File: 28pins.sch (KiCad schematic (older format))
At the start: 2 parts

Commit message: Adds 10-pin SIP header, BOM data to components
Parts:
- removed U?: ATMEGA16U2, symbol ATMEGA16U2
- added U?: ATMEGA16U2-AU, 28pins:TQFP-32_7x7mm_Pitch0.8mm, symbol ATMEGA16U2-AU
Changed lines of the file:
@@
 LIBS:valves
 LIBS:28pins
+LIBS:28pins-cache
 EELAYER 25 0
 EELAYER END
@@
 $EndComp
 $Comp
-L ATMEGA16U2 U?
-U 1 1 583FCE18
-P 11075 9775
-F 0 "U?" H 12125 9300 60  0000 C CNN
-F 1 "ATMEGA16U2" H 11025 9300 60  0000 C CNN
-F 2 "" H 12475 11075 60  0001 C CNN
-F 3 "" H 12475 11075 60  0001 C CNN
-	1    11075 9775
+L ATMEGA16U2-AU U?
+U 1 1 5840678A
+P 11525 9700
+F 0 "U?" H 12575 9225 60  0000 C CNN
+F 1 "ATMEGA16U2-AU" H 11475 9225 60  0000 C CNN
+F 2 "28pins:TQFP-32_7x7mm_Pitch0.8mm" H 11775 9025 60  0001 C CNN
+F 3 "http://www.atmel.com/Images/7799s.pdf" H 11750 8775 60  0001 C CNN
+F 4 "ATMEGA16U2-AU" H 11750 8575 60  0001 C CNN "MFG P/N"
+F 5 "Atmel" H 11100 8575 60  0001 C CNN "MFG"
+	1    11525 9700
 	1    0    0    -1
 $EndComp

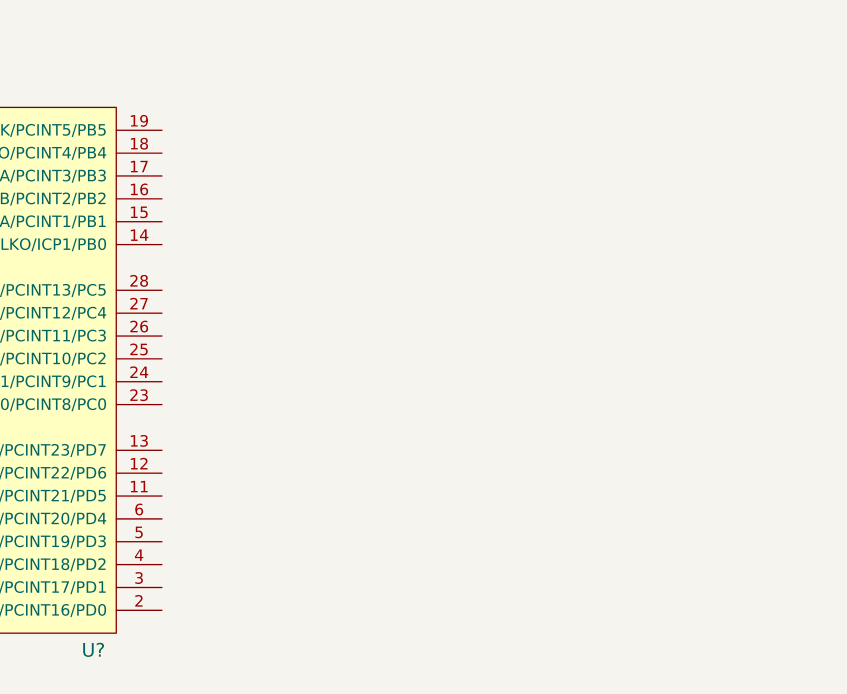
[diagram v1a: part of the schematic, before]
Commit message: Adds more headers and an 0805 capacitor
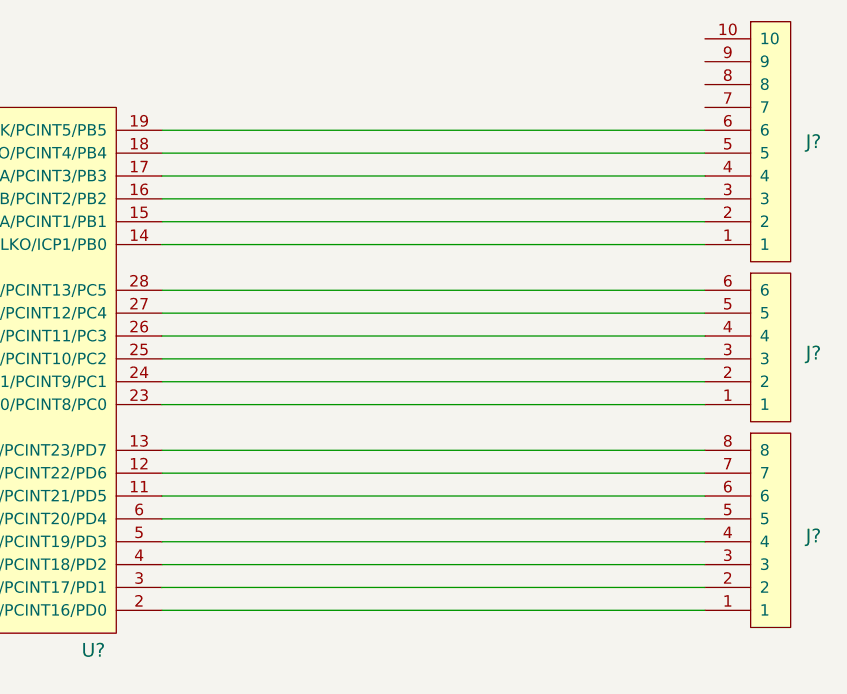
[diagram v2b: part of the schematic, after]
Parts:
- added J?: 10x1F, 28pins:1x10F_hdr, symbol 10x1F
- added J?: 8x1F, 28pins:1x10F_hdr, symbol 8x1F
- added J?: 6x1F, 28pins:1x6F_hdr, symbol 6x1F
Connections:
- net at U?.11 (OC0B/T1/PCINT21/PD5): now also J?.6
- net at U?.12 (OC0A/AIN0/PCINT22/PD6): now also J?.7
- net at U?.13 (AIN1/PCINT23/PD7): now also J?.8
- net at U?.14 (PCINT0/CLKO/ICP1/PB0): now also J?.1
- net at U?.15 (OC1A/PCINT1/PB1): now also J?.2
- net at U?.16 (SS/OC1B/PCINT2/PB2): now also J?.3
- net at U?.17 (MOSI/OC2A/PCINT3/PB3): now also J?.4
- net at U?.18 (MISO/PCINT4/PB4): now also J?.5
- net at U?.19 (SCK/PCINT5/PB5): now also J?.6
- net at U?.2 (RXD/PCINT16/PD0): now also J?.1
- net at U?.23 (ADC0/PCINT8/PC0): now also J?.1
- net at U?.24 (ADC1/PCINT9/PC1): now also J?.2
- net at U?.25 (ADC2/PCINT10/PC2): now also J?.3
- net at U?.26 (ADC3/PCINT11/PC3): now also J?.4
- net at U?.27 (ADC4/SDA/PCINT12/PC4): now also J?.5
- net at U?.28 (ADC5/SCL/PCINT13/PC5): now also J?.6
- net at U?.3 (TXD/PCINT17/PD1): now also J?.2
- net at U?.4 (INT0/PCINT18/PD2): now also J?.3
- net at U?.5 (OC2B/INT1/PCINT19/PD3): now also J?.4
- net at U?.6 (XCK/T0/PCINT20/PD4): now also J?.5
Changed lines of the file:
@@
 	1    0    0    -1
 $EndComp
+$Comp
+L 10x1F J?
+U 1 1 58410F8F
+P 20825 7675
+F 0 "J?" H 21100 7900 60  0000 C CNN
+F 1 "10x1F" H 20900 8475 60  0001 C CNN
+F 2 "28pins:1x10F_hdr" H 20800 7200 60  0001 C CNN
+F 3 "https://cdn.harwin.com/pdfs/M20-782.pdf" H 21025 6975 60  0001 C CNN
+F 4 "Harwin" H 20875 7075 60  0001 C CNN "MFG"
+F 5 "M20-7821042" H 21500 7075 60  0001 C CNN "MFG P/N"
+	1    20825 7675
+	1    0    0    1
+$EndComp
+$Comp
+L 8x1F J?
+U 1 1 58411004
+P 20825 9275
+F 0 "J?" H 21100 9625 60  0000 C CNN
+F 1 "8x1F" H 20900 10075 60  0001 C CNN
+F 2 "28pins:1x10F_hdr" H 20800 8800 60  0001 C CNN
+F 3 "https://cdn.harwin.com/pdfs/M20-782.pdf" H 21025 8575 60  0001 C CNN
+F 4 "Harwin" H 20875 8675 60  0001 C CNN "MFG"
+F 5 "M20-7820842" H 21500 8675 60  0001 C CNN "MFG P/N"
+	1    20825 9275
+	1    0    0    1
+$EndComp
+$Comp
+L 6x1F J?
+U 1 1 584110C3
+P 20825 8375
+F 0 "J?" H 21100 8825 60  0000 C CNN
+F 1 "6x1F" H 20900 9175 60  0001 C CNN
+F 2 "28pins:1x6F_hdr" H 20800 7900 60  0001 C CNN
+F 3 "https://cdn.harwin.com/pdfs/M20-782.pdf" H 21025 7675 60  0001 C CNN
+F 4 "Harwin" H 20875 7775 60  0001 C CNN "MFG"
+F 5 "M20-7820646" H 21500 7775 60  0001 C CNN "MFG P/N"
+	1    20825 8375
+	1    0    0    1
+$EndComp
+Wire Wire Line
+	18250 9850 20625 9850
+Wire Wire Line
+	18250 9950 20625 9950
+Wire Wire Line
+	18250 9650 20625 9650
+Wire Wire Line
+	18250 9750 20625 9750
+Wire Wire Line
+	18250 9450 20625 9450
+Wire Wire Line
+	18250 9550 20625 9550
+Wire Wire Line
+	18250 9250 20625 9250
+Wire Wire Line
+	18250 9350 20625 9350
+Wire Wire Line
+	18250 8950 20625 8950
+Wire Wire Line
+	18250 9050 20625 9050
+Wire Wire Line
+	18250 8750 20625 8750
+Wire Wire Line
+	18250 8850 20625 8850
+Wire Wire Line
+	18250 8550 20625 8550
+Wire Wire Line
+	18250 8650 20625 8650
+Wire Wire Line
+	18250 8250 20625 8250
+Wire Wire Line
+	18250 8350 20625 8350
+Wire Wire Line
+	18250 8050 20625 8050
+Wire Wire Line
+	18250 8150 20625 8150
+Wire Wire Line
+	18250 7850 20625 7850
+Wire Wire Line
+	18250 7950 20625 7950
 $EndSCHEMATC

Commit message: Moar components
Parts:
- added C? (x17): 100n, 28pins:C_0805, symbol 100n
- added C? (x5): 10u, 28pins:C_1206, symbol 10u
- added C? (x4): 18p, 28pins:C_0805, symbol 18p
- added D? (x2): BAT54HT1G, symbol BAT54HT1G
- added D? (x3): LO-L29K-H2K1-24-Z, 28pins:LED_0603, symbol LO-L29K-H2K1-24-Z
- added D?: LG-L29K-F2J1-24-Z, 28pins:LED_0603, symbol LG-L29K-F2J1-24-Z
- added E? (x3): MPZ2012S601AT000, 28pins:C_0805, symbol MPZ2012S601AT000
- added J?: 8x1F, 28pins:1x10F_hdr, symbol 8x1F
- added JP?: 3x1F, 28pins:Pin_Header_Straight_1x03, symbol 3x1F
- added P? (x2): CONN_02X03, 28pins:Pin_Header_Straight_2x03, symbol CONN_02X03
- added P?: CONN_02X02, 28pins:Pin_Header_Straight_2x02, symbol CONN_02X02
- added P?: CONN_01X04, 28pins:Pin_Header_Straight_1x04, symbol CONN_01X04
- added R? (x2): 1M, 28pins:R_0805, symbol 1M
- added R? (x4): 22R, 28pins:R_0805, symbol 22R
- added R? (x3): 1k, 28pins:R_0805, symbol 1k
- added R? (x5): 10k, 28pins:R_0805, symbol 10k
- added R? (x4): 560R, 28pins:R_0805, symbol 560R
- added S?: SPST_MOM_NO, 28pins:Pin_Header_Straight_2x02, symbol SPST_MOM_NO
- added U? (x3): SN74AHC1G09DBVR, 28pins:SOT-23-5, symbol SN74AHC1G09DBVR
- added Y? (x2): 16MHz, 28pins:Y_5X3.2, symbol 16MHz
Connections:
- net labels added: +3.3V, +5V, +5V/+3V3, 16U2PROG_328P_RESETn, 16U2_BUF_RESETn, 16U2_HDR_RESETn, 16U2_MISO, 16U2_MOSI, 16U2_PB4, 16U2_PB5, 16U2_PB6, 16U2_PB7, 16U2_RESETn, 16U2_RXD, 16U2_SCK, 16U2_SCK_R, 16U2_TXD, 328P_AUTORESETn, 328P_BUF_RESETn, 328P_RESETn, AD0, AD1, AD2, AD3, AD4/SDA, AD5/SCL, AREF, BUTTON_RESETn, GND, GNDREF, IO0, IO1, IO2, IO3, IO4, IO5, IO6, IO7, IO8, IO9, MISO, MOSI, PWRLED, RXLED, SCK, SCKLED, SCK_R, SS, TXLED
- wire segments 20 -> 211
- no-connect marks 0 -> 2
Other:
- moved on the sheet: J?, U?

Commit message: Almost done
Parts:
- added C? (x2): 10u, 28pins:C_1206, symbol 10u
- added C?: 1u, 28pins:C_0805, symbol 1u
- added C? (x2): 100u, 28pins:C_6.3MM_POL_SMD, symbol 100u
- added C? (x2): 100n, 28pins:C_0805, symbol 100n
- added FID? (x4): FIDUCIAL_1MM, symbol FIDUCIAL_1MM
- added J?: 3x1F, 28pins:Pin_Header_Straight_1x03, symbol 3x1F
- added J? (x2): PAD_WITH_HOLE, 28pins:PAD_WITH_HOLE, symbol PAD_WITH_HOLE
- added L?: 2u2, 28pins:L1210, symbol 2u2
- added MH? (x3): MOUNTING_HOLE, 28pins:MOUNTING_HOLE_PLATED, symbol MOUNTING_HOLE
- added MH?: MOUNTING_HOLE_NP, 28pins:MOUNTING_HOLE_NP, symbol MOUNTING_HOLE_NP
- added P?: 10118192-0001LF, 28pins:10118192-0001LF, symbol 10118192-0001LF
- added R? (x4): 0R, 28pins:R_0805, symbol 0R
- added R?: 100k, 28pins:R_0805, symbol 100k
- added R? (x3): 22R, 28pins:R_0805, symbol 22R
- added R? (x2): CG0603MLC-05E, 28pins:R_0603, symbol CG0603MLC-05E
- added R?: 10k, 28pins:R_0805, symbol 10k
- added R?: 560R, 28pins:R_0805, symbol 560R
- added S?: SPST_MOM_NO, 28pins:Pin_Header_Straight_2x02, symbol SPST_MOM_NO
- added U?: TL1963A-33DCQR, 28pins:SOT223-6, symbol TL1963A-33DCQR
- added U?: SN74AHC1G09DBVR, 28pins:SOT-23-5, symbol SN74AHC1G09DBVR
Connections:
- net labels added: +5/3V3_16U2, +5/3V3_16U2_UCAP, +5/3V3_328P_AVCC, +5/3V3_328P_VCC, +5V_USB, 16U2_RXLED, 16U2_TXLED, 16U2_USB_N, 16U2_USB_P, 16U2_XTAL1, 16U2_XTAL2, 328P_XTAL1, 328P_XTAL2, BUF_USER_BUTTON, CON_USB_N, CON_USB_P, USER_BUTTON
- net labels removed: RXLED, TXLED
- wire segments 211 -> 277
- no-connect marks 2 -> 11
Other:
- note added: "NF"
- note added: "VOLTAGE SELECTION"
- moved on the sheet: R?
